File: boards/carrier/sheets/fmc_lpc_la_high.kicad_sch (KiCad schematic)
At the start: 1 part, among them J4B FX10A-168P-SV(91)

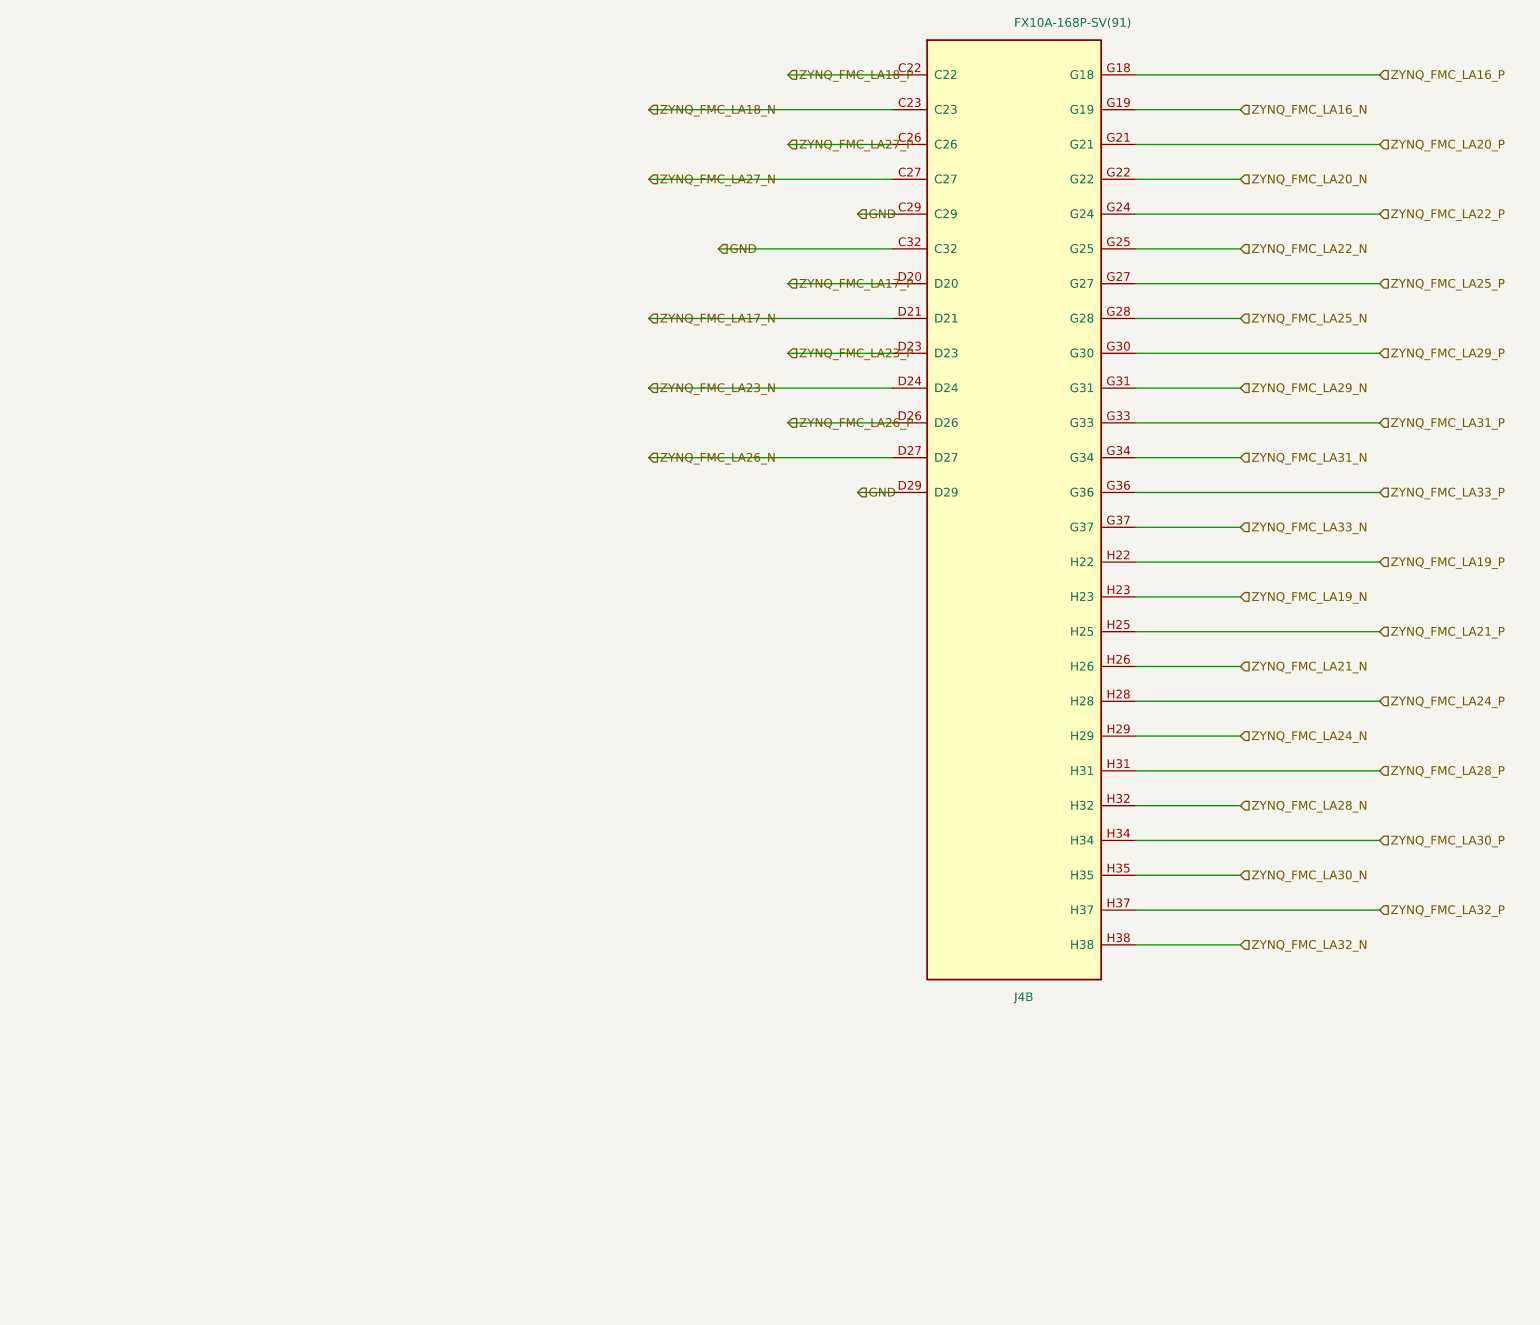
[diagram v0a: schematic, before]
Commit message: clean build: overlap=0 bounds=0 ERC=0 on all 27 sheets
Drives the carrier to a fully clean build — every sheet passes the
strict overlap/bounds validators AND KiCad ERC with 0 errors, nothing
hidden. Finishes the correctness + faithful-validators + placement
overhaul.

Geometry / placement (general algorithms, no per-block patches):

* _add_wire_with_bbox: partial-collinear-overlap clip. A new wire that
  partially overlaps an existing collinear wire (neither exact-dup nor
  subset) is clipped by interval-subtraction to its uncovered residual
  and meets the covering wire at a shared endpoint (validator-exempt,
  KiCad-merged). Removes the usb_pd doubled-trunk overlap; connectivity
  is preserved exactly.

* pick_dynamic_value_shift: generic fallback ladder. When a lib_id has
  no curated VALUE_SHIFT entry (connectors, power symbols, arbitrary
  ICs) the baseline is synthesised from the symbol's own library Value
  position (_library_value_shift), so the refinement can relocate ANY
  overlapping Value text. _refine_cluster_value_shifts now acts on every
  conflicting symbol except #PWR/#FLG (whose rail label is positional).
  Clears the jtag J2 part-name vs GND-symbol value overprint.

ERC errors 5 -> 0 (real electrical fixes, no rule suppression):

* PWR_FLAG Rule B (geometry-aware): the root index exposes no sheet
  pins, so hier-label nets are LOCAL per sub-sheet. Any DECLARED net
  carrying an IC power-INPUT pin (read from symbol pin TYPE), that is
  not a global power-symbol rail and has no local driver, now gets a
  local PWR_FLAG. Fixes power/usbc_otg +VIN (LDO/switch IN) and hdmi_rx
  VCCB (cable-side 5V sense). +3V3/+5V stay exempt (global, driven by a
  flag elsewhere).

* Decoupling-array eligibility is now per-part: a part whose from_pin
  has no NAMED net (e.g. the CP2102N reset pull-up onto bare ~{RST})
  stays clustered on its pin instead of being arrayed with an
  unlabelable terminal. Fixes uart_bridge R102 dangling pin.

* Connector cluster/array d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
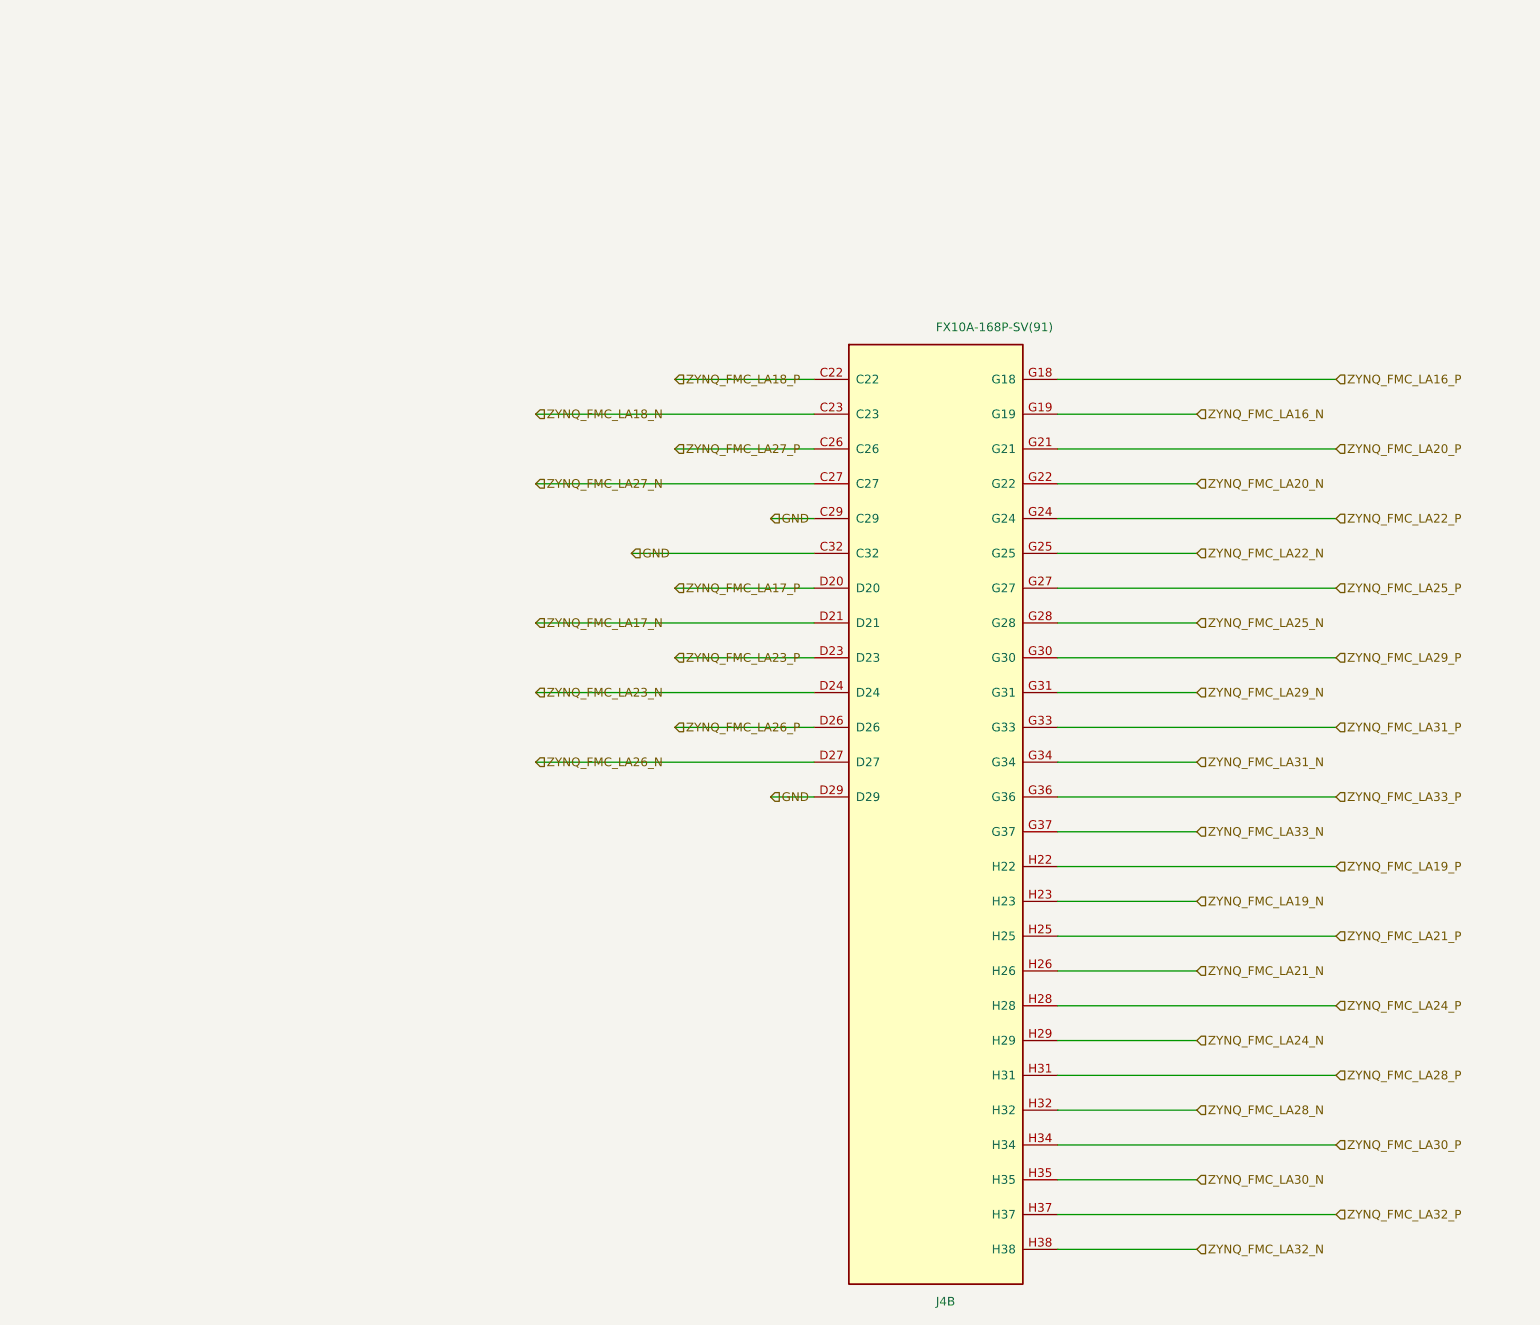
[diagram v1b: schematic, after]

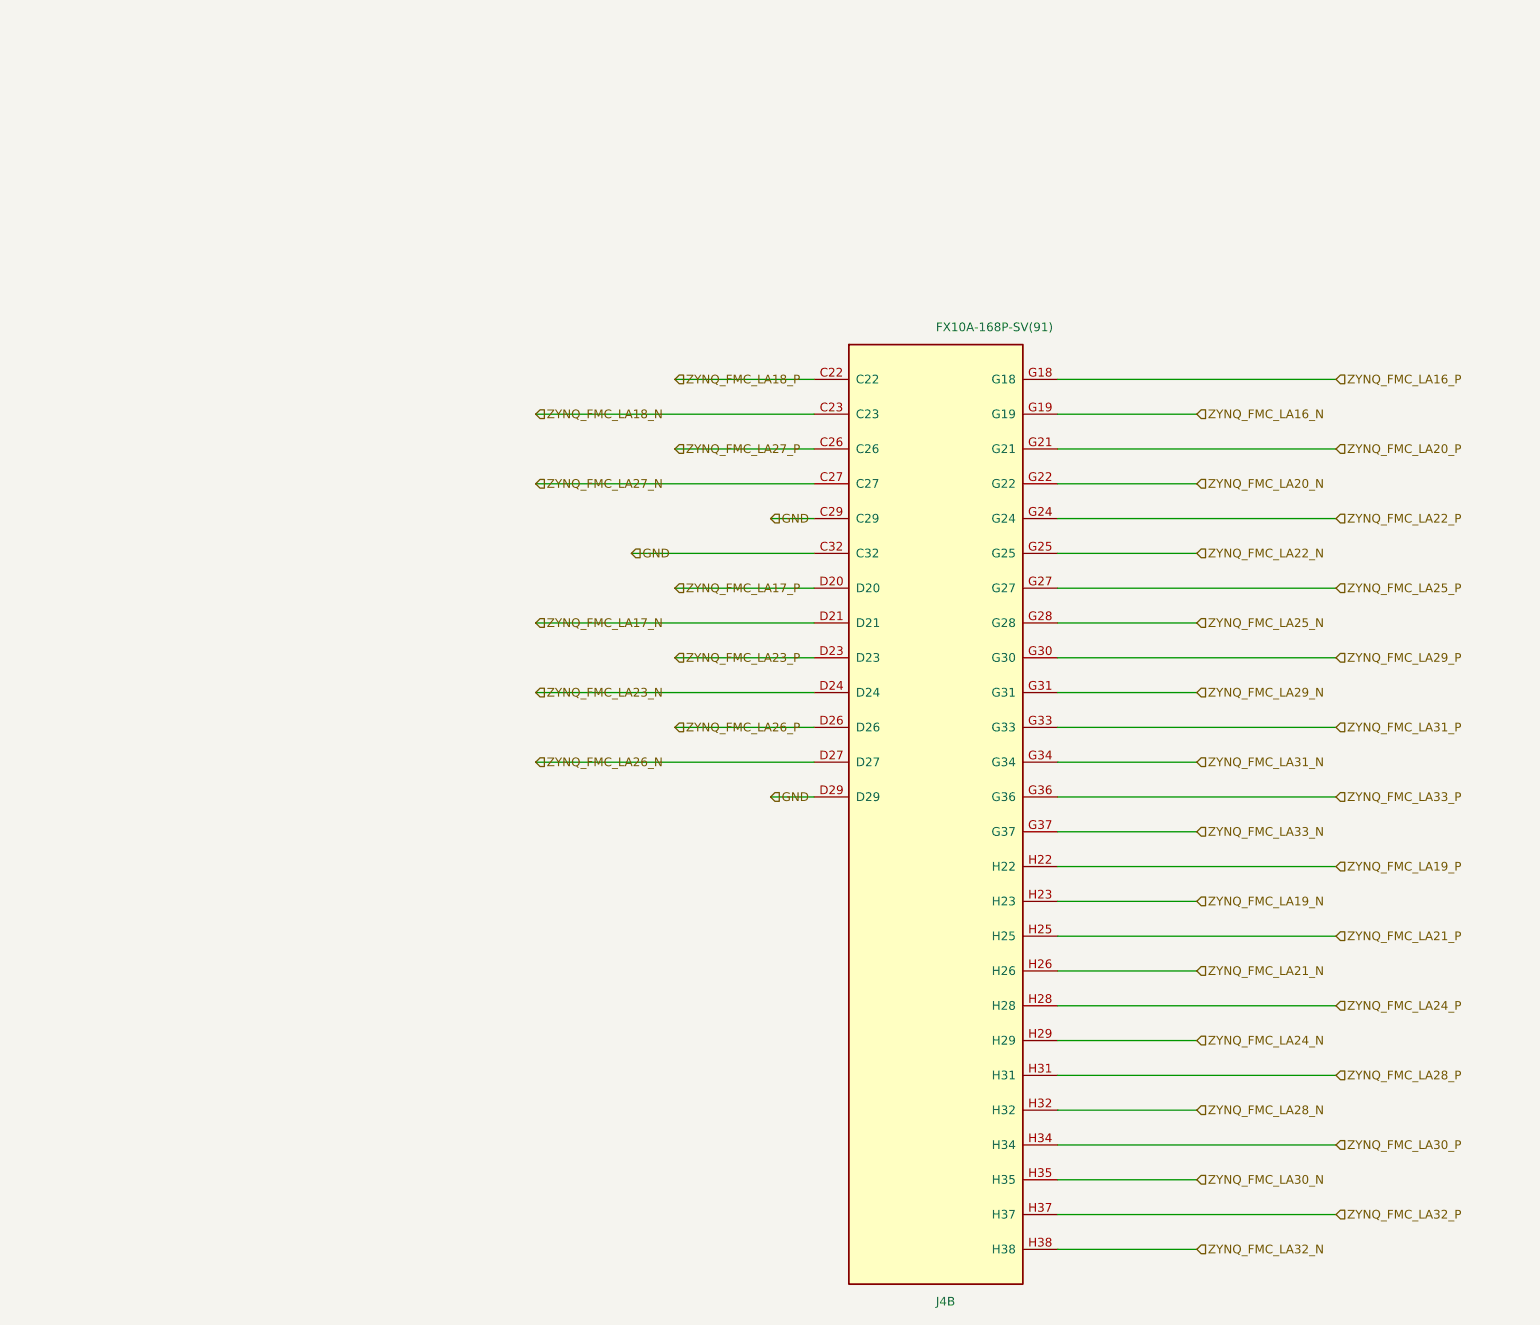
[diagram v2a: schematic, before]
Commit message: Regenerate carrier (overlap=0 all 27, ERC 134->22) + STAGE_E_STATUS UPDATE 4
Co-Authored-By: Claude Opus 4.8 <noreply@anthropic.com>
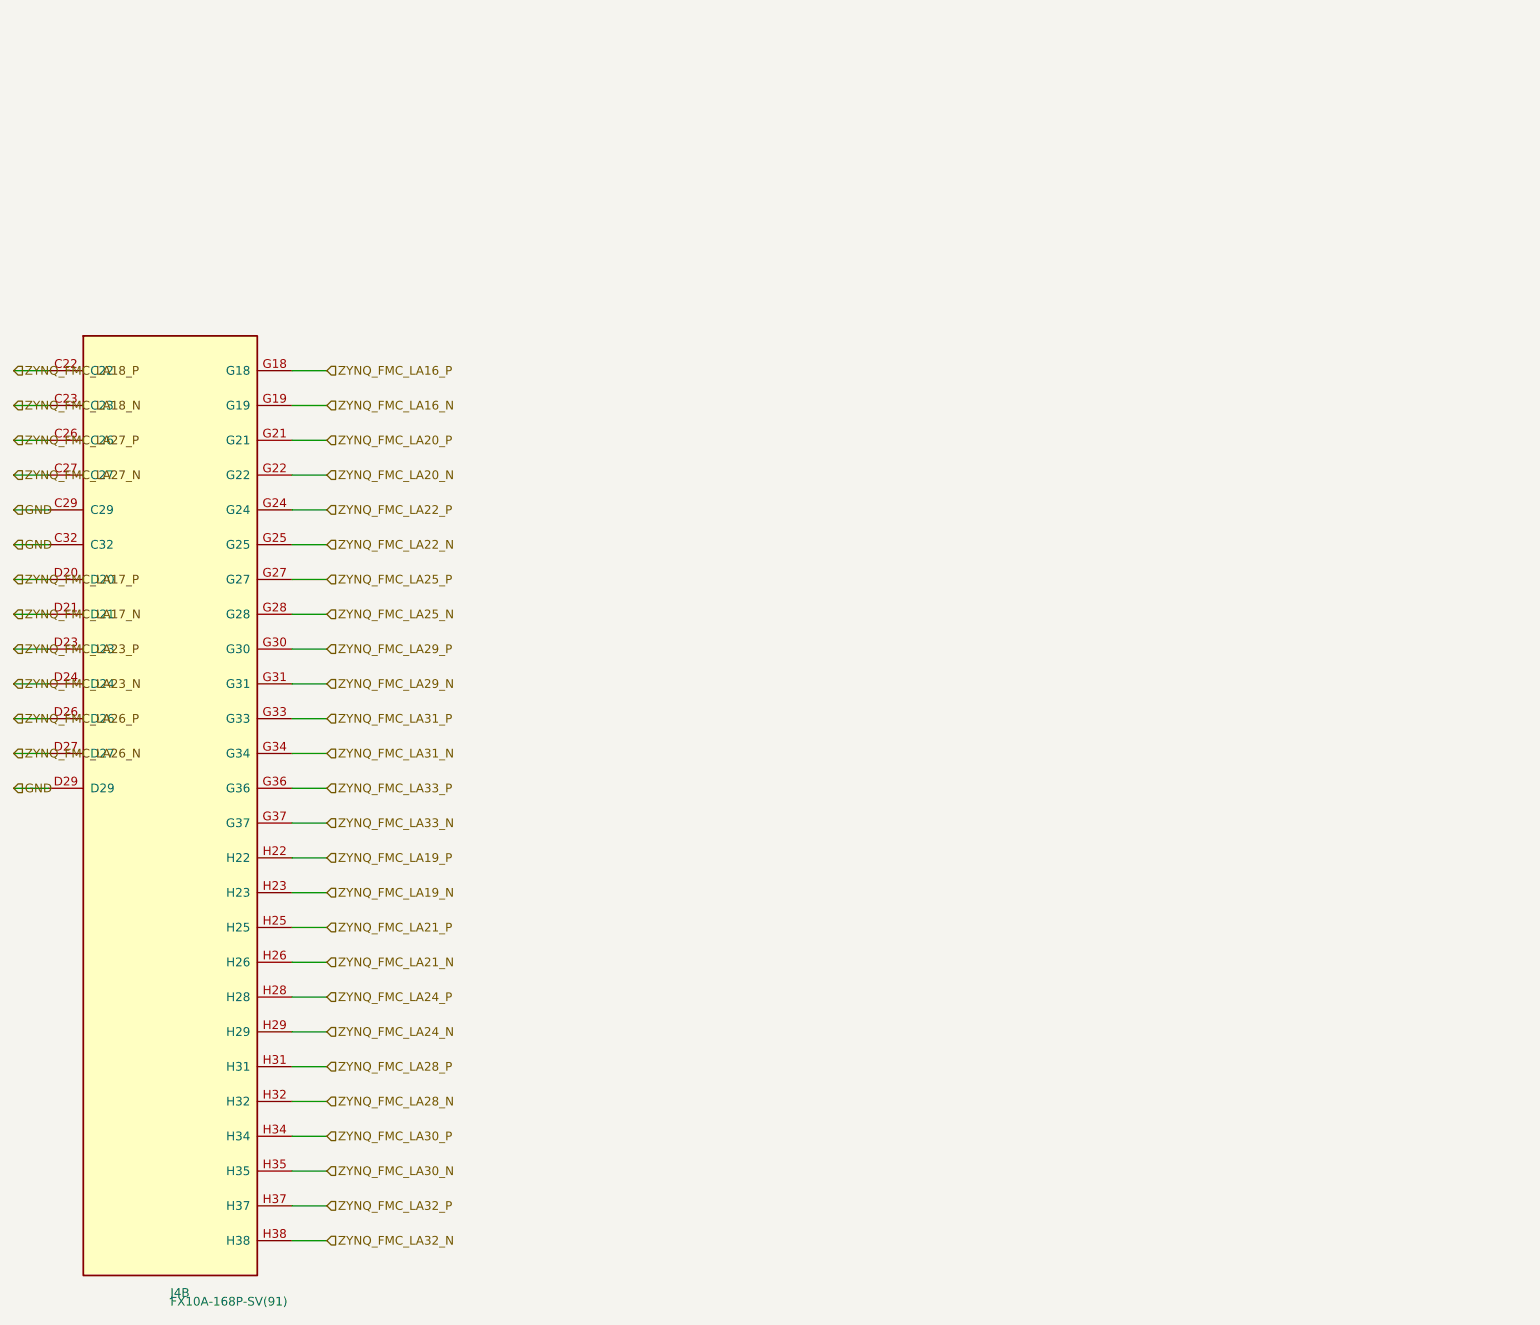
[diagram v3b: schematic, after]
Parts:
- J4B: LCSC C6624664 -> (none)
